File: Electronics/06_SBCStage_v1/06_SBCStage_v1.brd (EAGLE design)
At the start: 100 x 80 mm, 33 parts, among them J3 CONN_2X3_SMD, J4 BARRIER_BLOCK-3PIN, U1 XL4016-DEV

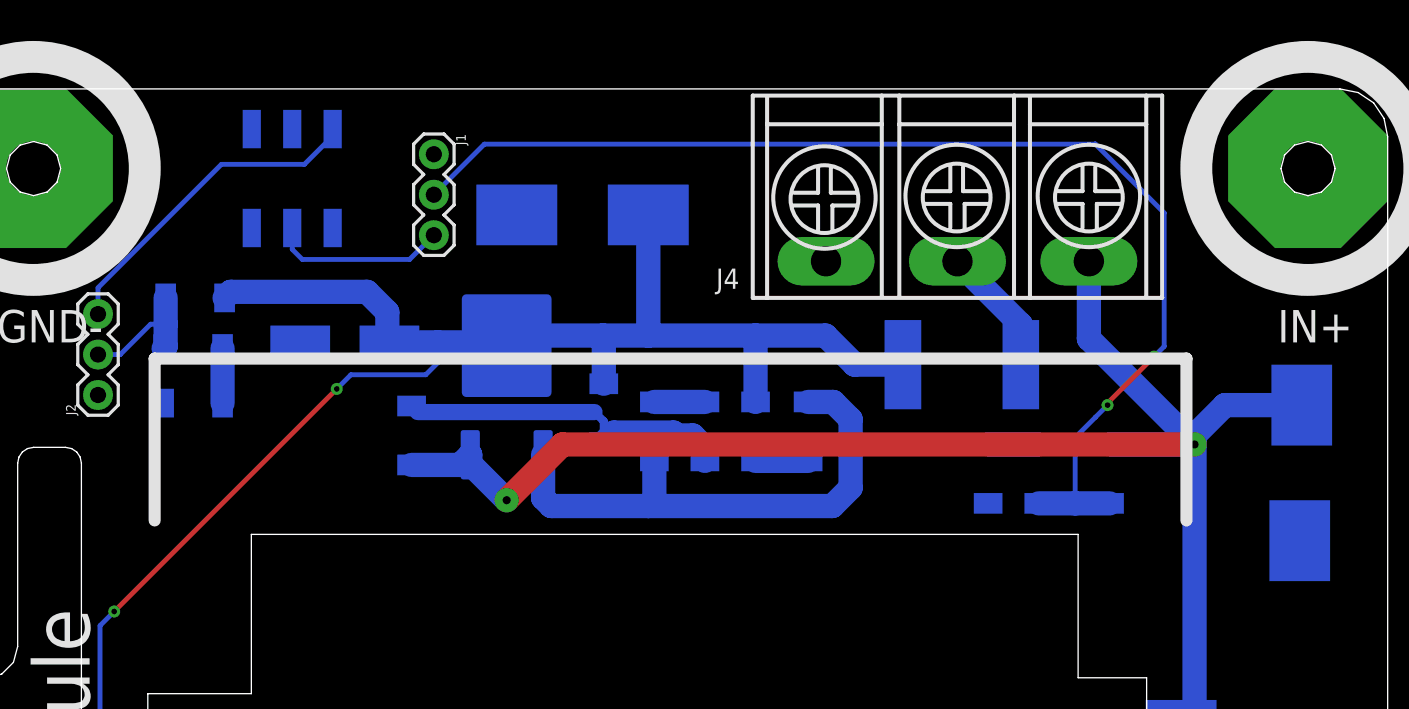
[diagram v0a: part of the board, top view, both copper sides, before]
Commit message: SBC stage: Moved test point to after the PTC fuse
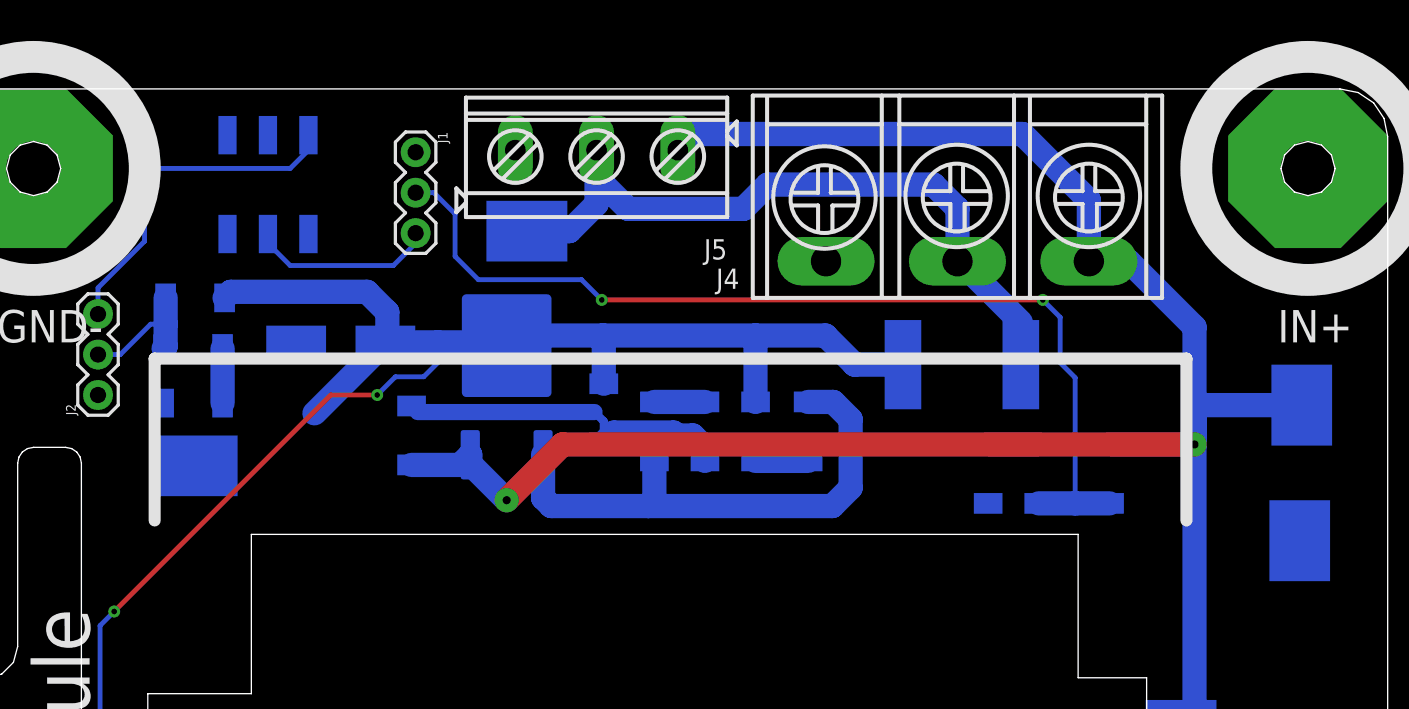
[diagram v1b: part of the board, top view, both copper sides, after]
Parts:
- added J5: SCREW_TERMINAL_3, EK's Parts:SCREW_TERM_3
- moved TP4 25.5 mm to (42.5, 74.5)
- moved TP7 7.69 mm to (63.2, 89.3), turned to 270 degrees
- moved J3 1.57 mm to (47.0, 92.2)
- moved J1 1.15 mm to (56.3, 94.2)
- moved U$2 0.25 mm to (51.6, 82.3)
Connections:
- net GND: now also J5.P$3
- net N$2: now also J5.P$2, TP7.P$1
- net OUT1: no longer TP7.P$1
- net V+: now also J5.P$1
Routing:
- net N$2: track 8.14 -> 43.8 mm
- net V+: track 167.3 -> 201.7 mm
- net SIG_SMPS: track 74.0 -> 61.8 mm
- net OUT1: track 158.9 -> 157.9 mm
- net N$7: track 20.8 -> 21.7 mm
- net N$9: track 11.1 -> 11.6 mm

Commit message: Naming update to Hippo-PD
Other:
- board text added: "hippo-pd sbc v1"
- board text removed: "hippo-ps sbc v1"
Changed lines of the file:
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@@
 <text x="88.265" y="92.456" size="1.524" layer="22" font="vector" ratio="20" rot="MR180">out1</text>
 <text x="80.264" y="92.456" size="1.524" layer="22" font="vector" ratio="20" rot="MR180">gnd</text>
-<text x="28.702" y="36.83" size="1.524" layer="22" font="vector" ratio="20" rot="MR90">hippo-ps sbc v1</text>
+<text x="28.702" y="36.83" size="1.524" layer="22" font="vector" ratio="20" rot="MR90">hippo-pd sbc v1</text>
 <text x="28.702" y="62.103" size="1.524" layer="22" font="vector" ratio="20" rot="MR90">ek robotgrrl Jul 13, '22</text>
 </plain>

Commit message: SBC stage electronics v1 final
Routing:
- net OUT1: track 157.9 -> 151.6 mm
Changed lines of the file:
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@@
 <drawing>
 <settings>
-<setting alwaysvectorfont="no"/>
+<setting alwaysvectorfont="yes"/>
 <setting verticaltext="up"/>
 </settings>
@@
 <text x="29.972" y="82.296" size="2.032" layer="21" font="vector" ratio="20">GND-</text>
 <text x="110.363" y="82.296" size="2.032" layer="21" font="vector" ratio="20">IN+</text>
-<text x="24.892" y="28.067" size="2.032" layer="22" font="vector" ratio="20" rot="MR0">IN+</text>
+<text x="34.544" y="32.258" size="2.032" layer="22" font="vector" ratio="20" rot="MR0">IN+</text>
 <text x="113.538" y="32.385" size="2.032" layer="22" font="vector" ratio="20" rot="MR0">GND-</text>
 <text x="113.919" y="82.423" size="2.032" layer="22" font="vector" ratio="20" rot="MR0">IN+</text>
-<text x="25.019" y="86.741" size="2.032" layer="22" font="vector" ratio="20" rot="MR0">GND-</text>
+<text x="36.449" y="82.296" size="2.032" layer="22" font="vector" ratio="20" rot="MR0">GND-</text>
 <text x="76.073" y="29.845" size="1.524" layer="22" font="vector" ratio="20" rot="MR270">swtch</text>
 <text x="68.199" y="29.337" size="1.524" layer="22" font="vector" ratio="20" rot="MR270">out1</text>
@@
 <text x="28.702" y="36.83" size="1.524" layer="22" font="vector" ratio="20" rot="MR90">hippo-pd sbc v1</text>
 <text x="28.702" y="62.103" size="1.524" layer="22" font="vector" ratio="20" rot="MR90">ek robotgrrl Jul 13, '22</text>
+<text x="28.702" y="53.086" size="1.524" layer="21" font="vector" ratio="20" rot="SR270">hippo-pd sbc v1</text>
+<text x="28.702" y="85.598" size="1.524" layer="21" font="vector" ratio="20" rot="SR270">ek robotgrrl Jul 13, '22</text>
 </plain>
 <attributes>
@@
 <wire x1="50.927" y1="78.994" x2="37.338" y2="65.405" width="0.3048" layer="1"/>
 <via x="53.848" y="78.994" extent="1-16" drill="0.35"/>
-<wire x1="54.362" y1="82.296" x2="49.911" y2="77.845" width="1.524" layer="16"/>
 <wire x1="68.022" y1="82.727" x2="77.597" y2="82.727" width="1.524" layer="16"/>
 </signal>
